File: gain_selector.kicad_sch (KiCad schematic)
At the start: 6 parts, among them Q11 NMOS, Q12 NMOS

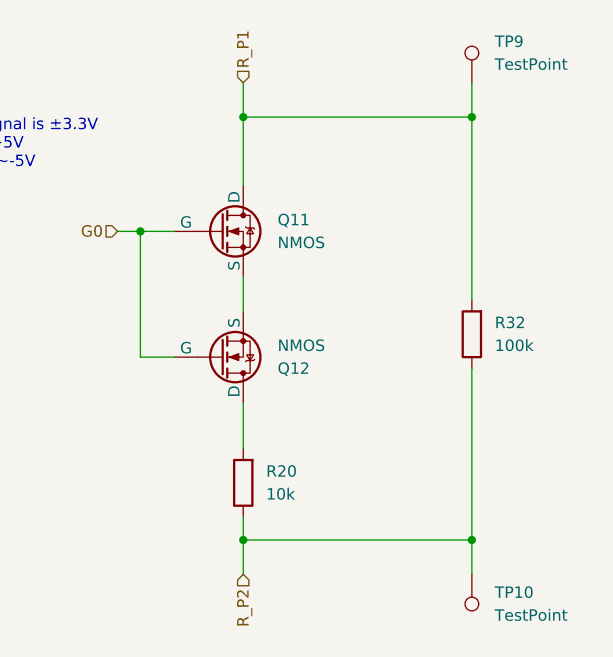
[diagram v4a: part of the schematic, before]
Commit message: Added protection to MCU analog inputs
DUT and test voltages now use clamping diodes to protect the MCU from
voltages less than 0V and greater than 3.3V.
Started laying out again, but thinking of trying something different
with the layou of the range resistors around the 1st opamp.
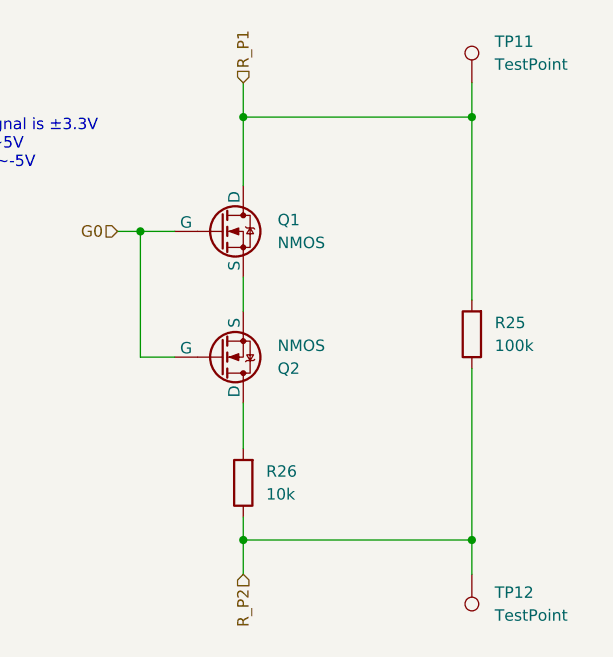
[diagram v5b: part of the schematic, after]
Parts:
- renumbered Q11 to Q1, Q12 to Q2, R32 to R25, R20 to R26, TP9 to TP11, TP10 to TP12
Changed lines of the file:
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@@
 		(dnp no)
 		(fields_autoplaced yes)
-		(property "Reference" "R32"
+		(property "Reference" "R25"
 			(at 115.57 55.8799 0)
 			(show_name no)
@@
 			(project "lcr"
 				(path "/226ea51e-4da2-4daa-967e-dce167947430/c9f416db-c7a0-48f3-8fda-35fdd9af5fe5/2911f1c4-2f69-429a-9438-24c6ac9b9c30"
-					(reference "R32")
+					(reference "R25")
 					(unit 1)
 				)
@@
 		(dnp no)
 		(fields_autoplaced yes)
-		(property "Reference" "TP9"
+		(property "Reference" "TP11"
 			(at 115.57 24.6379 0)
 			(show_name no)
@@
 			(project "lcr"
 				(path "/226ea51e-4da2-4daa-967e-dce167947430/c9f416db-c7a0-48f3-8fda-35fdd9af5fe5/2911f1c4-2f69-429a-9438-24c6ac9b9c30"
-					(reference "TP9")
+					(reference "TP11")
 					(unit 1)
 				)
@@
 		(in_pos_files yes)
 		(dnp no)
-		(property "Reference" "Q12"
+		(property "Reference" "Q2"
 			(at 91.44 60.9601 0)
 			(show_name no)
@@
 			(project "lcr"
 				(path "/226ea51e-4da2-4daa-967e-dce167947430/c9f416db-c7a0-48f3-8fda-35fdd9af5fe5/2911f1c4-2f69-429a-9438-24c6ac9b9c30"
-					(reference "Q12")
+					(reference "Q2")
 					(unit 1)
 				)
@@
 		(dnp no)
 		(fields_autoplaced yes)
-		(property "Reference" "Q11"
+		(property "Reference" "Q1"
 			(at 91.44 44.4499 0)
 			(show_name no)
@@
 			(project "lcr"
 				(path "/226ea51e-4da2-4daa-967e-dce167947430/c9f416db-c7a0-48f3-8fda-35fdd9af5fe5/2911f1c4-2f69-429a-9438-24c6ac9b9c30"
-					(reference "Q11")
+					(reference "Q1")
 					(unit 1)
 				)
@@
 		(dnp no)
 		(fields_autoplaced yes)
-		(property "Reference" "TP10"
+		(property "Reference" "TP12"
 			(at 115.57 85.8519 0)
 			(show_name no)
@@
 			(project "lcr"
 				(path "/226ea51e-4da2-4daa-967e-dce167947430/c9f416db-c7a0-48f3-8fda-35fdd9af5fe5/2911f1c4-2f69-429a-9438-24c6ac9b9c30"
-					(reference "TP10")
+					(reference "TP12")
 					(unit 1)
 				)
@@
 		(dnp no)
 		(fields_autoplaced yes)
-		(property "Reference" "R20"
+		(property "Reference" "R26"
 			(at 90.17 72.3899 0)
 			(show_name no)
@@
 			(project "lcr"
 				(path "/226ea51e-4da2-4daa-967e-dce167947430/c9f416db-c7a0-48f3-8fda-35fdd9af5fe5/2911f1c4-2f69-429a-9438-24c6ac9b9c30"
-					(reference "R20")
+					(reference "R26")
 					(unit 1)
 				)

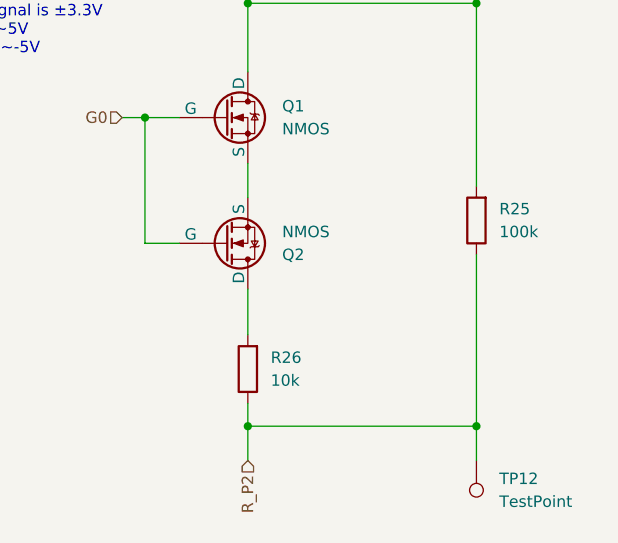
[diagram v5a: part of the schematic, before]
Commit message: Added gate drive current limiting resistors
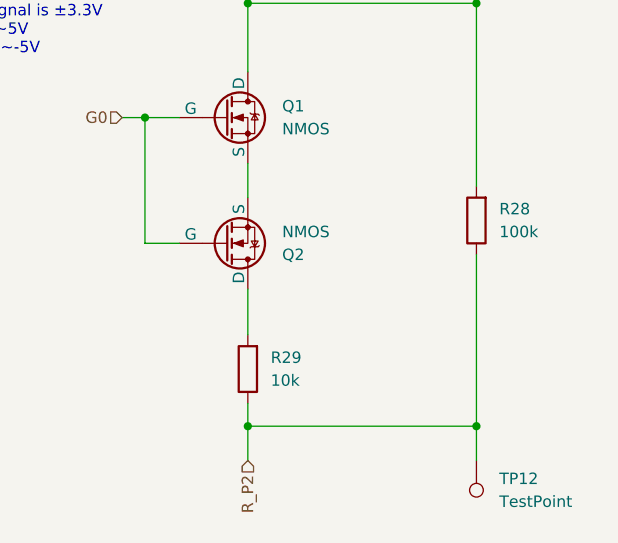
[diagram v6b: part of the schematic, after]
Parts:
- renumbered R25 to R28, R26 to R29
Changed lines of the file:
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@@
 		(dnp no)
 		(fields_autoplaced yes)
-		(property "Reference" "R25"
+		(property "Reference" "R28"
 			(at 115.57 55.8799 0)
 			(show_name no)
@@
 			(project "lcr"
 				(path "/226ea51e-4da2-4daa-967e-dce167947430/c9f416db-c7a0-48f3-8fda-35fdd9af5fe5/2911f1c4-2f69-429a-9438-24c6ac9b9c30"
-					(reference "R25")
+					(reference "R28")
 					(unit 1)
 				)
@@
 		(dnp no)
 		(fields_autoplaced yes)
-		(property "Reference" "R26"
+		(property "Reference" "R29"
 			(at 90.17 72.3899 0)
 			(show_name no)
@@
 			(project "lcr"
 				(path "/226ea51e-4da2-4daa-967e-dce167947430/c9f416db-c7a0-48f3-8fda-35fdd9af5fe5/2911f1c4-2f69-429a-9438-24c6ac9b9c30"
-					(reference "R26")
+					(reference "R29")
 					(unit 1)
 				)
